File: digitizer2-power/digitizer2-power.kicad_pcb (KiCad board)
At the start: 4 copper layers, 51 x 33 mm, 47 parts, among them P1 CONN_01X04, P2 CONN_02X04, U1 ADP2301, U2 ADP2301, U3 ADP2301, U4 ADP2301

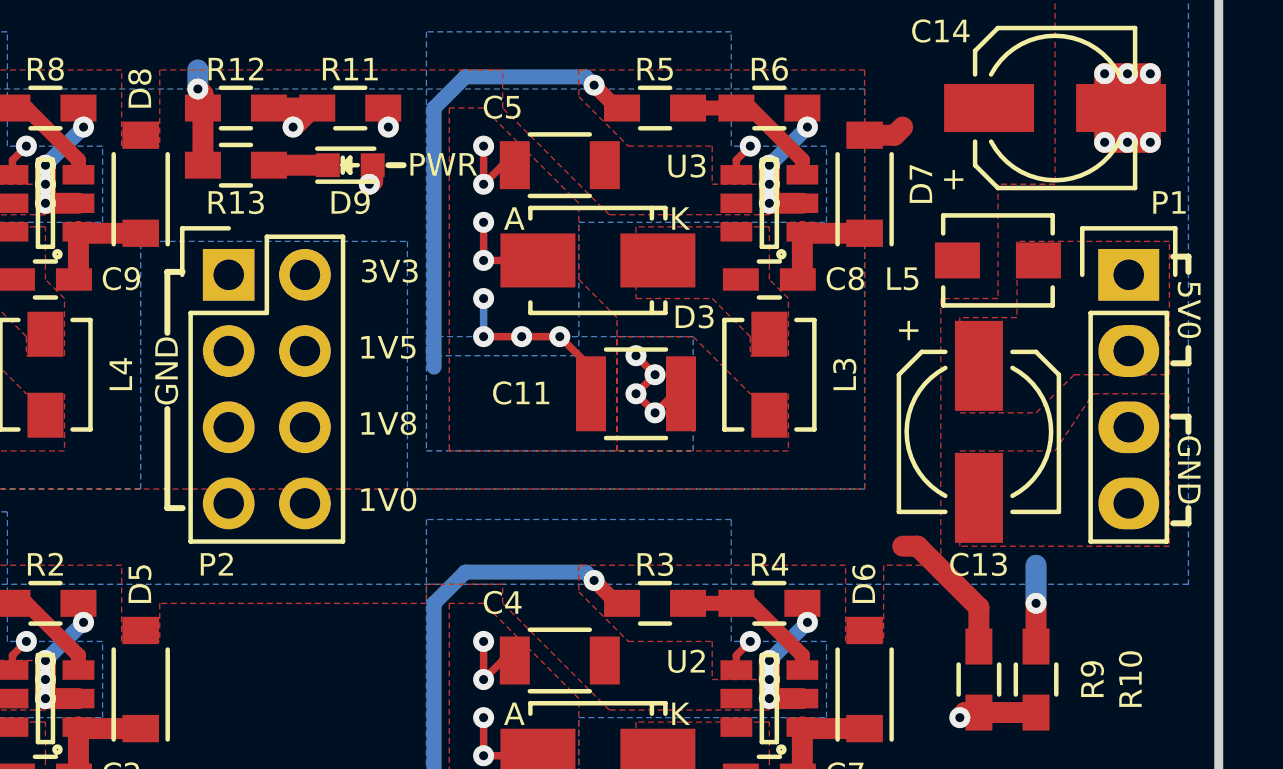
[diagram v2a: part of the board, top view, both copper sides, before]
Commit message: Fill in last details for power supply, cleanup
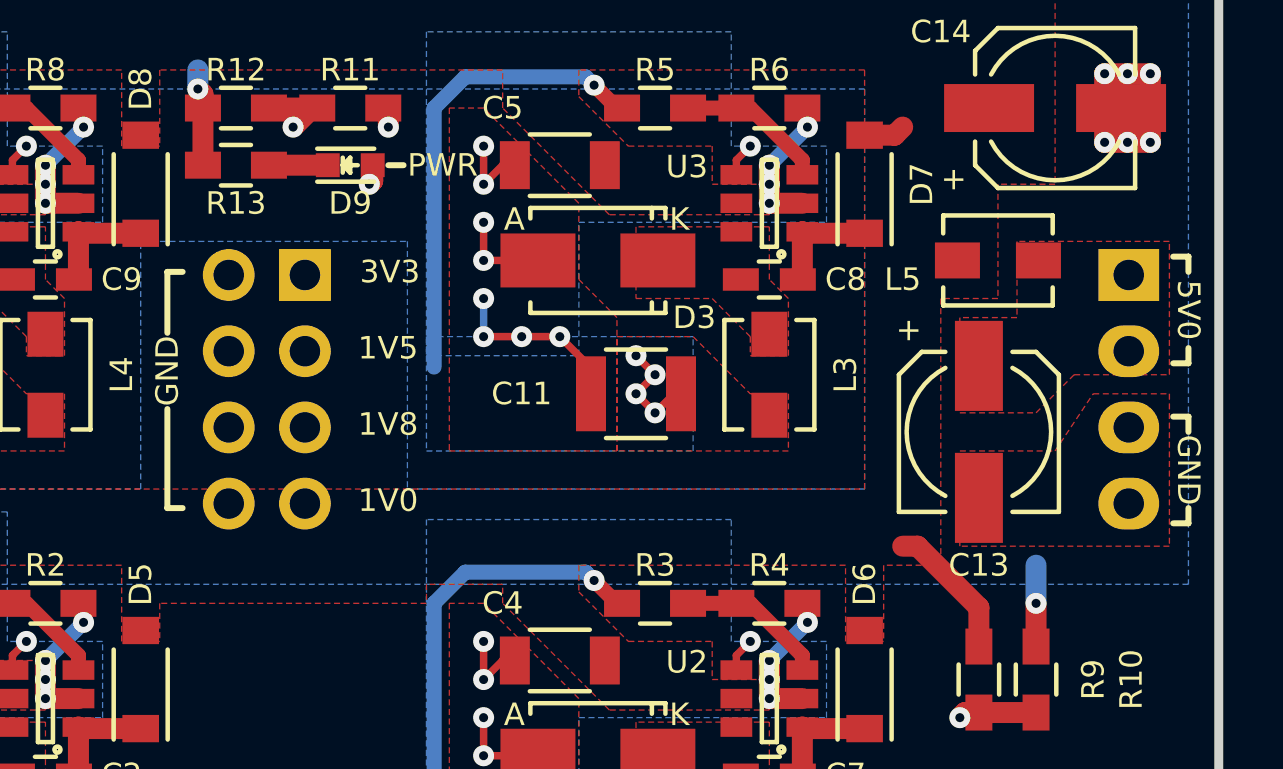
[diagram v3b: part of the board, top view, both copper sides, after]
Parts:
- C10, C11, C12, C3: value C_Small -> 47uF
- C13, C14: value C_Small -> 220uF
- P1, P2: moved to B.Cu
- R1: value div1 -> 3k
- R10, R12: value Ren2 -> 12k
- R11: value Ren1 -> 3k
- R2, R4: value div2 -> 12k
- R3: value div1 -> 15k
- R5: value div1 -> 13k
- R6, R8: value div2 -> 15k
- R7: value div1 -> 47k
- R9: value Ren1 -> 30k
- moved P2 2.54 mm to (152.2, 84.9), turned to 180 degrees
- turned P1 to 180 degrees
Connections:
- P2 pad 1: GND -> /3V3
- P2 pad 2: /3V3 -> GND
- P2 pad 3: GND -> /1V5
- P2 pad 4: /1V5 -> GND
- P2 pad 5: GND -> /1V8
- P2 pad 6: /1V8 -> GND
- P2 pad 7: GND -> /1V0
- P2 pad 8: /1V0 -> GND
